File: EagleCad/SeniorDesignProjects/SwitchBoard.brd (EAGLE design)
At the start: 160 x 100 mm, 10 parts

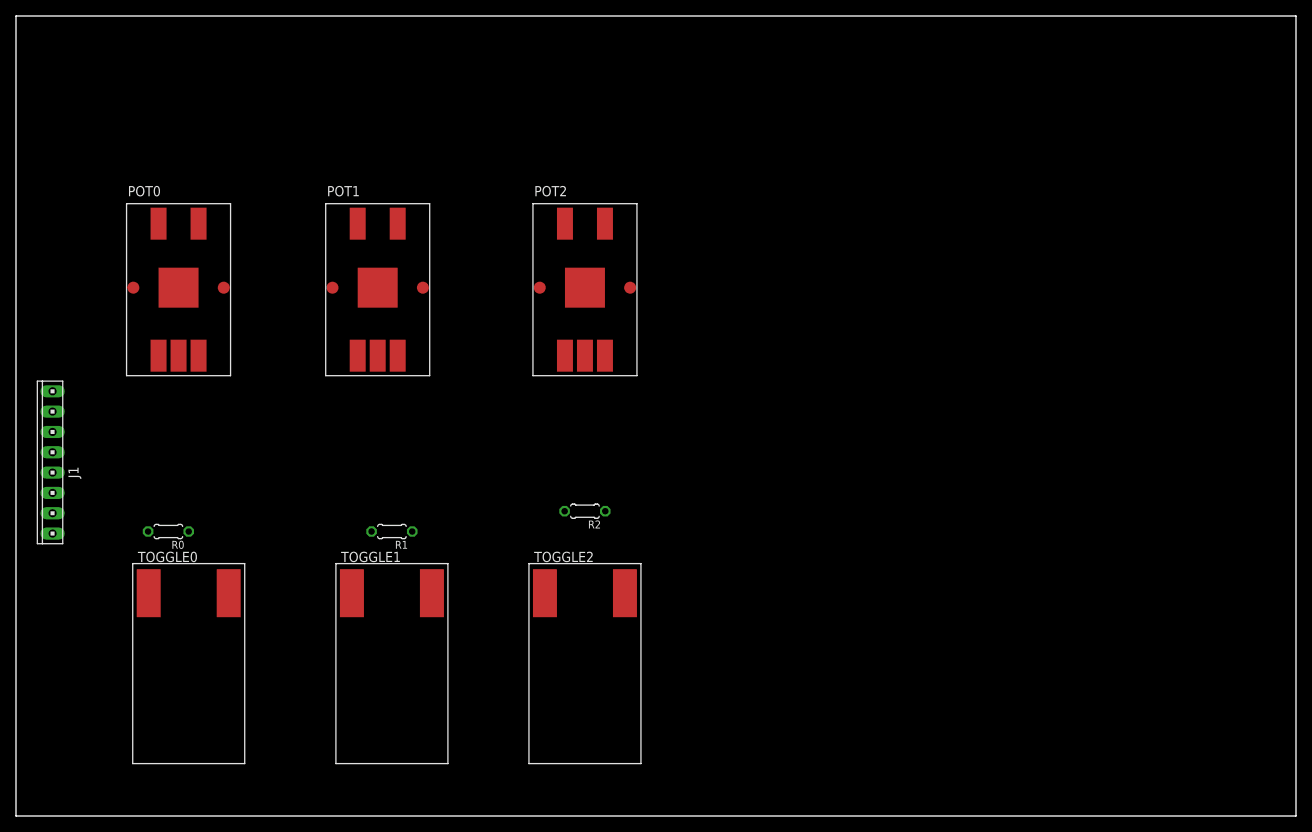
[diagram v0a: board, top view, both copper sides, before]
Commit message: Finished Switch Board schematic and Board layout
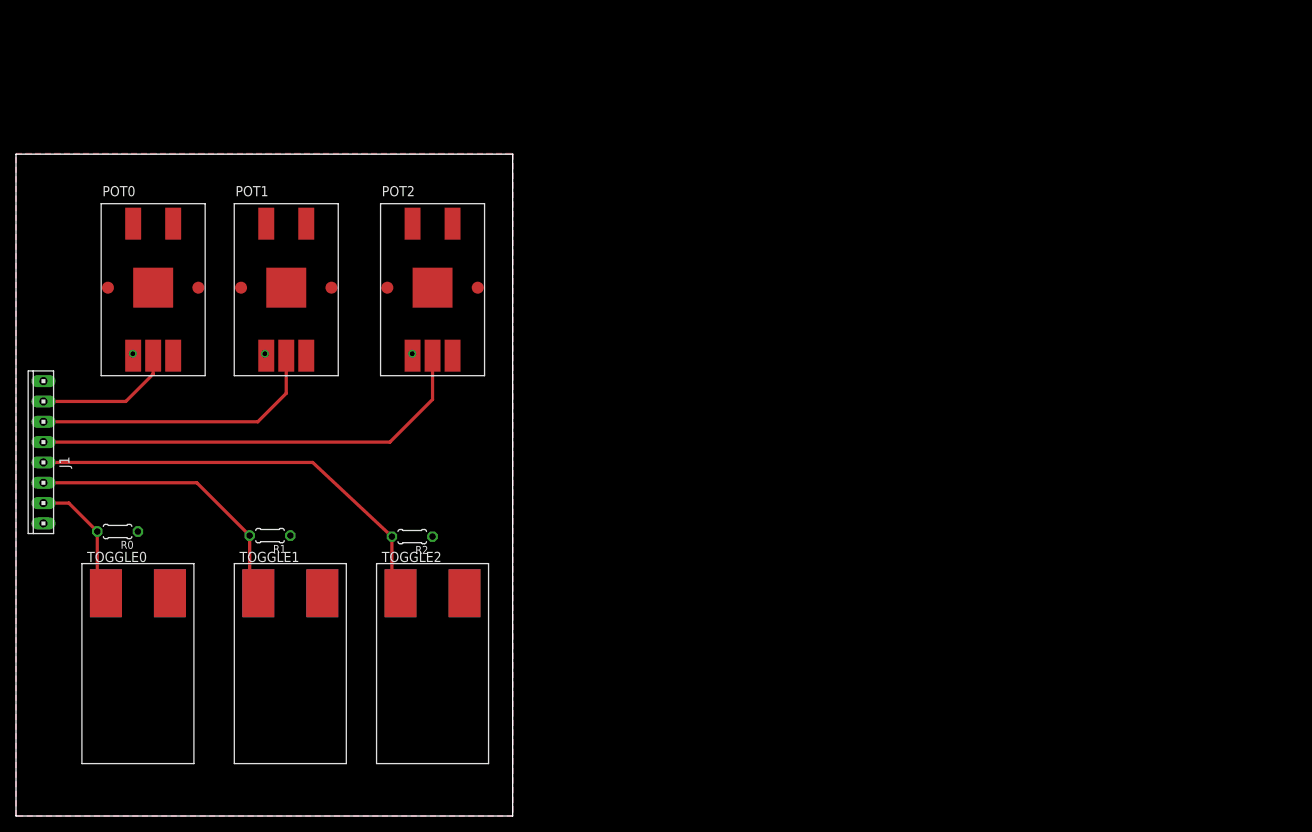
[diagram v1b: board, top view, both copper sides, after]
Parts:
- moved R2 21.8 mm to (49.5, 34.9)
- moved POT2 19.1 mm to (52.1, 66.0)
- moved TOGGLE2 19.1 mm to (52.1, 19.1)
- moved R1 15.2 mm to (31.8, 35.1)
- moved TOGGLE1 12.7 mm to (34.3, 19.1)
- moved POT1 11.4 mm to (33.8, 66.0)
- moved R0 6.35 mm to (12.7, 35.6)
- moved TOGGLE0 6.35 mm to (15.2, 19.1)
- moved POT0 3.18 mm to (17.1, 66.0)
- moved J1 1.71 mm to (3.43, 45.5)
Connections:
- net POT0: now also J1.2; no longer J1.4
- net POT2: now also J1.4; no longer J1.2
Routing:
- net POT2: track 0.00 -> 56.3 mm
- net TOGGLE2: track 0.00 -> 54.7 mm
- net POT1: track 0.00 -> 36.5 mm
- net TOGGLE1: track 0.00 -> 36.2 mm
- net POT0: track 0.00 -> 17.4 mm
- net TOGGLE0: track 0.00 -> 16.4 mm
- added copper zone on layer 16, net GND
- added copper zone on layer 1, net VCC
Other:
- board size 160 x 100 mm -> 62.1 x 82.7 mm
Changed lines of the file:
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@@
 <setting verticaltext="up"/>
 </settings>
-<grid distance="0.01" unitdist="inch" unit="inch" style="lines" multiple="1" display="no" altdistance="0.025" altunitdist="inch" altunit="inch"/>
+<grid distance="0.125" unitdist="inch" unit="inch" style="lines" multiple="1" display="yes" altdistance="0.025" altunitdist="inch" altunit="inch"/>
 <layers>
 <layer number="1" name="Top" color="4" fill="1" visible="yes" active="yes"/>
@@
 <board>
 <plain>
-<wire x1="0" y1="0" x2="160" y2="0" width="0" layer="20"/>
-<wire x1="160" y1="0" x2="160" y2="100" width="0" layer="20"/>
-<wire x1="160" y1="100" x2="0" y2="100" width="0" layer="20"/>
-<wire x1="0" y1="100" x2="0" y2="0" width="0" layer="20"/>
+<wire x1="0" y1="0" x2="62.083" y2="0" width="0" layer="20"/>
+<wire x1="62.083" y1="0" x2="62.083" y2="82.728" width="0" layer="20"/>
+<wire x1="62.083" y1="82.728" x2="0" y2="82.728" width="0" layer="20"/>
+<wire x1="0" y1="82.728" x2="0" y2="0" width="0" layer="20"/>
 </plain>
 <attributes>
@@
 </autorouter>
 <elements>
-<element name="R1" library="rcl" package="0204/5" value="" x="46.99" y="35.56" rot="R180"/>
-<element name="TOGGLE0" library="PhysicalSwitches" package="SPST-TOGGLE-SWITCH" value="COM-09276" x="21.59" y="19.05"/>
-<element name="TOGGLE1" library="PhysicalSwitches" package="SPST-TOGGLE-SWITCH" value="COM-09276" x="46.99" y="19.05"/>
-<element name="TOGGLE2" library="PhysicalSwitches" package="SPST-TOGGLE-SWITCH" value="COM-09276" x="71.12" y="19.05"/>
-<element name="POT0" library="PhysicalSwitches" package="POT-SMD" value="PRS11S-11" x="20.32" y="66.04"/>
-<element name="POT1" library="PhysicalSwitches" package="POT-SMD" value="PRS11S-11" x="45.212" y="66.04"/>
-<element name="POT2" library="PhysicalSwitches" package="POT-SMD" value="PRS11S-11" x="71.12" y="66.04"/>
-<element name="J1" library="con-amp" package="10X08MTA" value="" x="4.572" y="44.196" rot="R90"/>
-<element name="R2" library="rcl" package="0204/5" value="" x="71.12" y="38.1" rot="R180"/>
-<element name="R0" library="rcl" package="0204/5" value="" x="19.05" y="35.56" rot="R180"/>
+<element name="R1" library="rcl" package="0204/5" value="" x="31.75" y="35.052" rot="R180"/>
+<element name="TOGGLE0" library="PhysicalSwitches" package="SPST-TOGGLE-SWITCH" value="COM-09276" x="15.24" y="19.05"/>
+<element name="TOGGLE1" library="PhysicalSwitches" package="SPST-TOGGLE-SWITCH" value="COM-09276" x="34.29" y="19.05"/>
+<element name="TOGGLE2" library="PhysicalSwitches" package="SPST-TOGGLE-SWITCH" value="COM-09276" x="52.07" y="19.05"/>
+<element name="POT0" library="PhysicalSwitches" package="POT-SMD" value="PRS11S-11" x="17.145" y="66.04"/>
+<element name="POT1" library="PhysicalSwitches" package="POT-SMD" value="PRS11S-11" x="33.782" y="66.04"/>
+<element name="POT2" library="PhysicalSwitches" package="POT-SMD" value="PRS11S-11" x="52.07" y="66.04"/>
+<element name="J1" library="con-amp" package="10X08MTA" value="" x="3.429" y="45.466" rot="R90"/>
+<element name="R2" library="rcl" package="0204/5" value="" x="49.53" y="34.925" rot="R180"/>
+<element name="R0" library="rcl" package="0204/5" value="" x="12.7" y="35.56" rot="R180"/>
 </elements>
 <signals>
@@
 <contactref element="R1" pad="2"/>
 <contactref element="J1" pad="6"/>
-<wire x1="41.99" y1="27.85" x2="44.45" y2="35.56" width="0" layer="19" extent="1-1"/>
-<wire x1="4.572" y1="40.386" x2="41.99" y2="27.85" width="0" layer="19" extent="1-1"/>
+<wire x1="3.429" y1="41.656" x2="22.606" y2="41.656" width="0.4064" layer="1"/>
+<wire x1="22.606" y1="41.656" x2="29.21" y2="35.052" width="0.4064" layer="1"/>
+<wire x1="29.21" y1="28.93" x2="30.29" y2="27.85" width="0.4064" layer="1"/>
+<wire x1="29.21" y1="35.052" x2="29.21" y2="28.93" width="0.4064" layer="1"/>
 </signal>
 <signal name="TOGGLE2">
@@
 <contactref element="TOGGLE2" pad="1"/>
 <contactref element="R2" pad="2"/>
-<wire x1="66.12" y1="27.85" x2="68.58" y2="38.1" width="0" layer="19" extent="1-1"/>
-<wire x1="4.572" y1="42.926" x2="66.12" y2="27.85" width="0" layer="19" extent="1-1"/>
+<wire x1="3.429" y1="44.196" x2="37.084" y2="44.196" width="0.4064" layer="1"/>
+<wire x1="37.084" y1="44.196" x2="46.99" y2="34.925" width="0.4064" layer="1"/>
+<wire x1="46.355" y1="29.845" x2="46.99" y2="29.21" width="0.4064" layer="1"/>
+<wire x1="46.99" y1="34.925" x2="46.99" y2="29.21" width="0.4064" layer="1"/>
+<wire x1="46.99" y1="29.21" x2="47.625" y2="28.575" width="0.4064" layer="1"/>
+<wire x1="47.625" y1="28.575" x2="48.07" y2="27.85" width="0" layer="19" extent="1-1"/>
 </signal>
 <signal name="GND">
@@
 <contactref element="R2" pad="1"/>
 <contactref element="R0" pad="1"/>
-<wire x1="73.66" y1="38.1" x2="68.62" y2="57.54" width="0" layer="19" extent="1-1"/>
-<wire x1="49.53" y1="35.56" x2="73.66" y2="38.1" width="0" layer="19" extent="1-1"/>
-<wire x1="42.712" y1="57.54" x2="49.53" y2="35.56" width="0" layer="19" extent="1-1"/>
-<wire x1="17.82" y1="57.54" x2="42.712" y2="57.54" width="0" layer="19" extent="1-1"/>
-<wire x1="4.572" y1="53.086" x2="17.82" y2="57.54" width="0" layer="19" extent="1-1"/>
-<wire x1="21.59" y1="35.56" x2="17.82" y2="57.54" width="0" layer="19" extent="1-1"/>
+<polygon width="0.254" layer="16" isolate="0.6096">
+<vertex x="0" y="0"/>
+<vertex x="0" y="82.804"/>
+<vertex x="62.103" y="82.804"/>
+<vertex x="62.103" y="0"/>
+</polygon>
+<via x="14.605" y="57.785" extent="1-16" drill="0.6" shape="square"/>
+<via x="31.115" y="57.785" extent="1-16" drill="0.6" shape="square"/>
+<via x="49.53" y="57.785" extent="1-16" drill="0.6" shape="square"/>
+<wire x1="49.53" y1="57.785" x2="49.57" y2="57.54" width="0" layer="19" extent="1-1"/>
+<wire x1="14.645" y1="57.54" x2="14.605" y2="57.785" width="0" layer="19" extent="1-1"/>
+<wire x1="31.282" y1="57.54" x2="31.115" y2="57.785" width="0" layer="19" extent="1-1"/>
 </signal>
 <signal name="VCC">
@@
 <contactref element="POT2" pad="3"/>
 <contactref element="J1" pad="8"/>
-<wire x1="47.712" y1="57.54" x2="73.62" y2="57.54" width="0" layer="19" extent="1-1"/>
-<wire x1="22.82" y1="57.54" x2="47.712" y2="57.54" width="0" layer="19" extent="1-1"/>
-<wire x1="4.572" y1="35.306" x2="22.82" y2="57.54" width="0" layer="19" extent="1-1"/>
-<wire x1="26.59" y1="27.85" x2="4.572" y2="35.306" width="0" layer="19" extent="1-1"/>
-<wire x1="51.99" y1="27.85" x2="26.59" y2="27.85" width="0" layer="19" extent="1-1"/>
-<wire x1="76.12" y1="27.85" x2="51.99" y2="27.85" width="0" layer="19" extent="1-1"/>
+<polygon width="0.254" layer="1" isolate="0.6096">
+<vertex x="0" y="0"/>
+<vertex x="0" y="82.804"/>
+<vertex x="62.103" y="82.804"/>
+<vertex x="62.103" y="0"/>
+</polygon>
 </signal>
 <signal name="TOGGLE0">
@@
 <contactref element="J1" pad="7"/>
 <contactref element="R0" pad="2"/>
-<wire x1="16.59" y1="27.85" x2="16.51" y2="35.56" width="0" layer="19" extent="1-1"/>
-<wire x1="4.572" y1="37.846" x2="16.51" y2="35.56" width="0" layer="19" extent="1-1"/>
+<wire x1="3.429" y1="39.116" x2="6.604" y2="39.116" width="0.4064" layer="1"/>
+<wire x1="6.604" y1="39.116" x2="10.16" y2="35.56" width="0.4064" layer="1"/>
+<wire x1="10.16" y1="28.93" x2="11.24" y2="27.85" width="0.4064" layer="1"/>
+<wire x1="10.16" y1="28.93" x2="10.16" y2="35.56" width="0.4064" layer="1"/>
 </signal>
 <signal name="POT0">
 <contactref element="POT0" pad="2"/>
-<contactref element="J1" pad="4"/>
-<wire x1="4.572" y1="45.466" x2="20.32" y2="57.54" width="0" layer="19" extent="1-1"/>
+<contactref element="J1" pad="2"/>
+<wire x1="3.429" y1="51.816" x2="13.716" y2="51.816" width="0.4064" layer="1"/>
+<wire x1="13.716" y1="51.816" x2="17.145" y2="55.245" width="0.4064" layer="1"/>
+<wire x1="17.145" y1="55.245" x2="17.145" y2="57.54" width="0.4064" layer="1"/>
 </signal>
 <signal name="POT1">
 <contactref element="POT1" pad="2"/>
 <contactref element="J1" pad="3"/>
-<wire x1="4.572" y1="48.006" x2="45.212" y2="57.54" width="0" layer="19" extent="1-1"/>
+<wire x1="3.429" y1="49.276" x2="30.226" y2="49.276" width="0.4064" layer="1"/>
+<wire x1="30.226" y1="49.276" x2="33.782" y2="52.832" width="0.4064" layer="1"/>
+<wire x1="33.782" y1="52.832" x2="33.782" y2="57.54" width="0.4064" layer="1"/>
 </signal>
 <signal name="POT2">
 <contactref element="POT2" pad="2"/>
-<contactref element="J1" pad="2"/>
-<wire x1="4.572" y1="50.546" x2="71.12" y2="57.54" width="0" layer="19" extent="1-1"/>
+<contactref element="J1" pad="4"/>
+<wire x1="3.429" y1="46.736" x2="46.736" y2="46.736" width="0.4064" layer="1"/>
+<wire x1="46.736" y1="46.736" x2="52.07" y2="52.07" width="0.4064" layer="1"/>
+<wire x1="52.07" y1="52.07" x2="52.07" y2="57.54" width="0.4064" layer="1"/>
 </signal>
 </signals>

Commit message: Fixed Toggle Switch package for board layout
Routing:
- net TOGGLE1: track 36.2 -> 40.1 mm
- net TOGGLE0: track 16.4 -> 20.3 mm
- net TOGGLE2: track 54.7 -> 58.6 mm
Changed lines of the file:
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@@
 <wire x1="3.429" y1="41.656" x2="22.606" y2="41.656" width="0.4064" layer="1"/>
 <wire x1="22.606" y1="41.656" x2="29.21" y2="35.052" width="0.4064" layer="1"/>
-<wire x1="29.21" y1="28.93" x2="30.29" y2="27.85" width="0.4064" layer="1"/>
+<wire x1="29.21" y1="28.93" x2="34.29" y2="26.924" width="0.4064" layer="1"/>
 <wire x1="29.21" y1="35.052" x2="29.21" y2="28.93" width="0.4064" layer="1"/>
 </signal>
@@
 <wire x1="3.429" y1="44.196" x2="37.084" y2="44.196" width="0.4064" layer="1"/>
 <wire x1="37.084" y1="44.196" x2="46.99" y2="34.925" width="0.4064" layer="1"/>
-<wire x1="46.355" y1="29.845" x2="46.99" y2="29.21" width="0.4064" layer="1"/>
 <wire x1="46.99" y1="34.925" x2="46.99" y2="29.21" width="0.4064" layer="1"/>
 <wire x1="46.99" y1="29.21" x2="47.625" y2="28.575" width="0.4064" layer="1"/>
-<wire x1="47.625" y1="28.575" x2="48.07" y2="27.85" width="0" layer="19" extent="1-1"/>
+<wire x1="47.625" y1="28.575" x2="52.07" y2="26.924" width="0.4064" layer="1"/>
 </signal>
 <signal name="GND">
@@
 <wire x1="3.429" y1="39.116" x2="6.604" y2="39.116" width="0.4064" layer="1"/>
 <wire x1="6.604" y1="39.116" x2="10.16" y2="35.56" width="0.4064" layer="1"/>
-<wire x1="10.16" y1="28.93" x2="11.24" y2="27.85" width="0.4064" layer="1"/>
+<wire x1="10.16" y1="28.93" x2="15.24" y2="26.924" width="0.4064" layer="1"/>
 <wire x1="10.16" y1="28.93" x2="10.16" y2="35.56" width="0.4064" layer="1"/>
 </signal>
